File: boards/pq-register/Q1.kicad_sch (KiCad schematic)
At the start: 92 parts, among them Q57 MMBT5401, Q58 MMBT5401, Q59 MMBT5401, Q60 MMBT5401, Q61 MMBT5401, Q62 MMBT5401, Q64 MMBT5401, Q66 MMBT5401, Q67 MMBT5401, Q68 MMBT5401, Q69 MMBT5401, Q70 MMBT5401, Q71 MMBT5401, Q72 MMBT5401

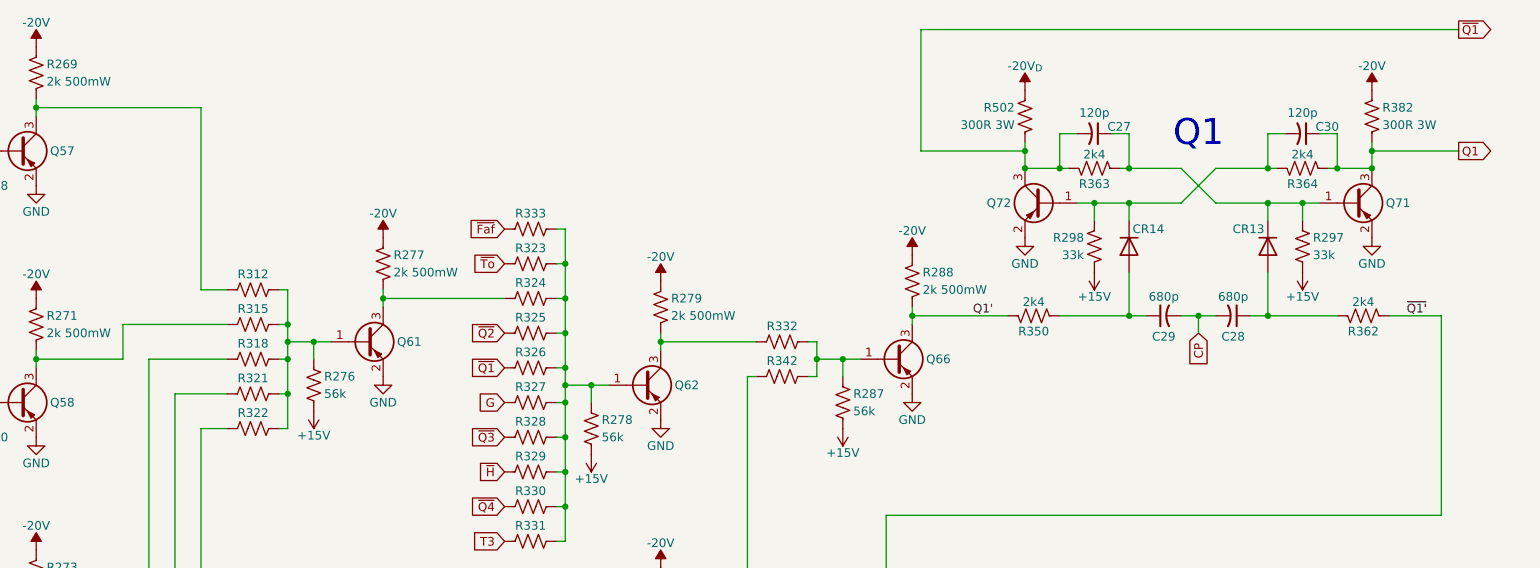
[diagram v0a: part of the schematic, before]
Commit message: Better PCI footprint, more layout.
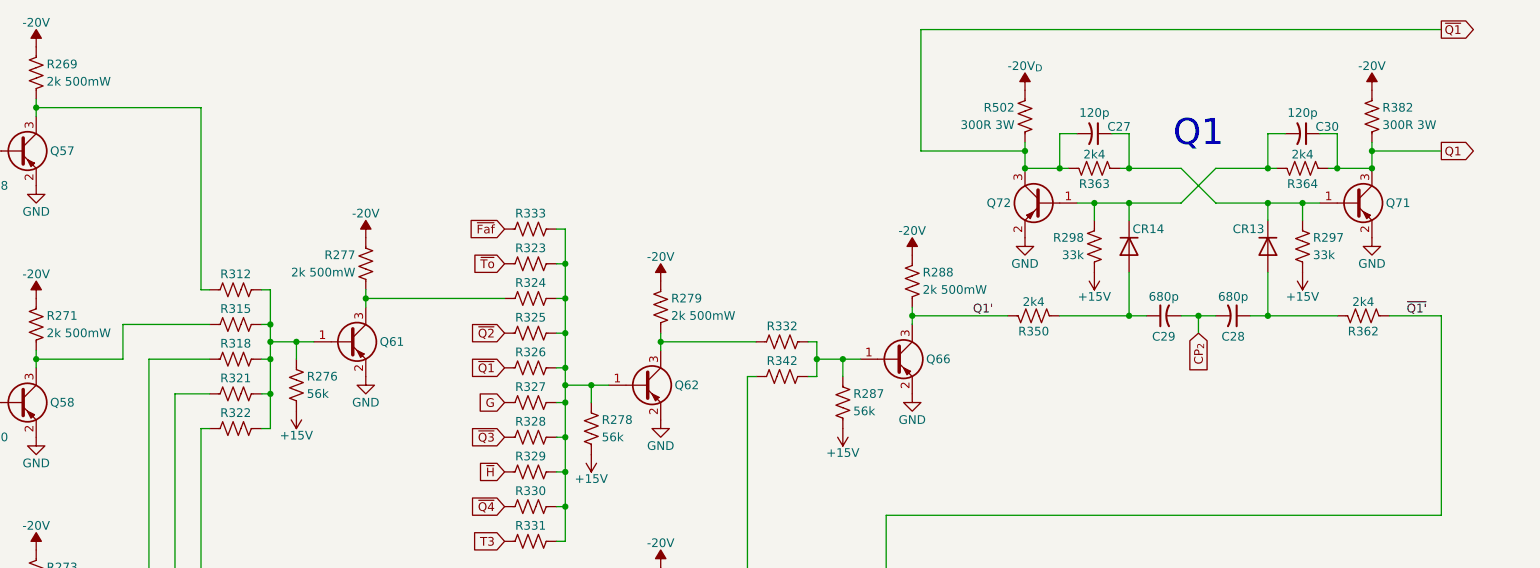
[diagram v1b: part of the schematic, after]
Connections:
- net CP renamed CP_{2}
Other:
- moved on the sheet: Q61, R276, R277, R312, R315, R318, R321, R322

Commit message: Start updating 2k4 resistors to 0603, melt some traces.
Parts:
- R269, R271, R273, R275, R277, R279, R284, R288, R290, R292, R294, R296: value 2k 500mW -> 2k ½W
- R350, R362, R363, R364: value 2k4 -> 2k4 ¼W; footprint Resistor_SMD:R_0402_1005Metric -> Resistor_SMD:R_0603_1608Metric
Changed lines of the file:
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@@
 			)
 		)
-		(property "Value" "2k 500mW"
+		(property "Value" "2k ½W"
 			(at 48.514 27.94 0)
 			(show_name no)
@@
 			)
 		)
-		(property "Value" "2k 500mW"
+		(property "Value" "2k ½W"
 			(at 139.954 62.23 0)
 			(show_name no)
@@
 			)
 		)
-		(property "Value" "2k 500mW"
+		(property "Value" "2k ½W"
 			(at 139.954 104.14 0)
 			(show_name no)
@@
 			)
 		)
-		(property "Value" "2k 500mW"
+		(property "Value" "2k ½W"
 			(at 48.514 64.77 0)
 			(show_name no)
@@
 			)
 		)
-		(property "Value" "2k 500mW"
+		(property "Value" "2k ½W"
 			(at 48.514 101.6 0)
 			(show_name no)
@@
 			)
 		)
-		(property "Value" "2k4"
+		(property "Value" "2k4 ¼W"
 			(at 241.3 60.198 90)
 			(show_name no)
@@
 			)
 		)
-		(property "Footprint" "Resistor_SMD:R_0402_1005Metric"
+		(property "Footprint" "Resistor_SMD:R_0603_1608Metric"
 			(at 241.554 63.246 90)
 			(hide yes)
@@
 			)
 		)
-		(property "Value" "2k 500mW"
+		(property "Value" "2k ½W"
 			(at 110.744 172.72 0)
 			(show_name no)
@@
 			)
 		)
-		(property "Value" "2k 500mW"
+		(property "Value" "2k ½W"
 			(at 48.514 175.26 0)
 			(show_name no)
@@
 			)
 		)
-		(property "Value" "2k 500mW"
+		(property "Value" "2k ½W"
 			(at 48.514 138.43 0)
 			(show_name no)
@@
 			)
 		)
-		(property "Value" "2k 500mW"
+		(property "Value" "2k ½W"
 			(at 162.814 137.16 0)
 			(show_name no)
@@
 			)
 		)
-		(property "Value" "2k 500mW"
+		(property "Value" "2k ½W"
 			(at 93.726 55.88 0)
 			(show_name no)
@@
 			)
 		)
-		(property "Value" "2k 500mW"
+		(property "Value" "2k ½W"
 			(at 176.784 58.42 0)
 			(show_name no)
@@
 			)
 		)
-		(property "Value" "2k4"
+		(property "Value" "2k4 ¼W"
 			(at 193.04 60.198 90)
 			(show_name no)
@@
 			)
 		)
-		(property "Footprint" "Resistor_SMD:R_0402_1005Metric"
+		(property "Footprint" "Resistor_SMD:R_0603_1608Metric"
 			(at 193.294 63.246 90)
 			(hide yes)
@@
 			)
 		)
-		(property "Value" "2k4"
+		(property "Value" "2k4 ¼W"
 			(at 201.93 38.608 90)
 			(show_name no)
@@
 			)
 		)
-		(property "Footprint" "Resistor_SMD:R_0402_1005Metric"
+		(property "Footprint" "Resistor_SMD:R_0603_1608Metric"
 			(at 202.184 41.656 90)
 			(hide yes)
@@
 			)
 		)
-		(property "Value" "2k4"
+		(property "Value" "2k4 ¼W"
 			(at 232.41 38.608 90)
 			(show_name no)
@@
 			)
 		)
-		(property "Footprint" "Resistor_SMD:R_0402_1005Metric"
+		(property "Footprint" "Resistor_SMD:R_0603_1608Metric"
 			(at 232.664 41.656 90)
 			(hide yes)
@@
 			)
 		)
-		(property "Value" "2k 500mW"
+		(property "Value" "2k ½W"
 			(at 110.744 135.89 0)
 			(show_name no)

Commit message: Clean up sheet frames.
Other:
- company: © 1962 General Precision; redrawn by Sam Hanes -> © 2026 Sam Hanes, licensed CERN-OHL-W v2
- title: LGP-21 P & Q Register Board -> LGP-21 Mini - P&Q Register
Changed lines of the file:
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@@
 	(generator "eeschema")
 	(generator_version "10.0")
-	(paper "A")
+	(paper "USLetter")
 	(title_block
-		(title "LGP-21 P & Q Register Board")
-		(date "2026-06-15")
-		(rev "ESD 1060")
-		(company "© 1962 General Precision; redrawn by Sam Hanes")
-		(comment 1 "https://github.com/Elemecca/lgp21-docs")
+		(title "LGP-21 Mini - P&Q Register")
+		(date "2026-06-28")
+		(rev "A")
+		(company "© 2026 Sam Hanes, licensed CERN-OHL-W v2")
+		(comment 1 "https://github.com/Elemecca/lgp21-mini")
 	)
 	(text "Q1"
